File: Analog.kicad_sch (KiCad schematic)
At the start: 32 parts, among them IC1 AMC1350DWVR, IC2 AMC1350DWVR, U3 TLV9001IDBVR, U4 TLV9001IDBVR

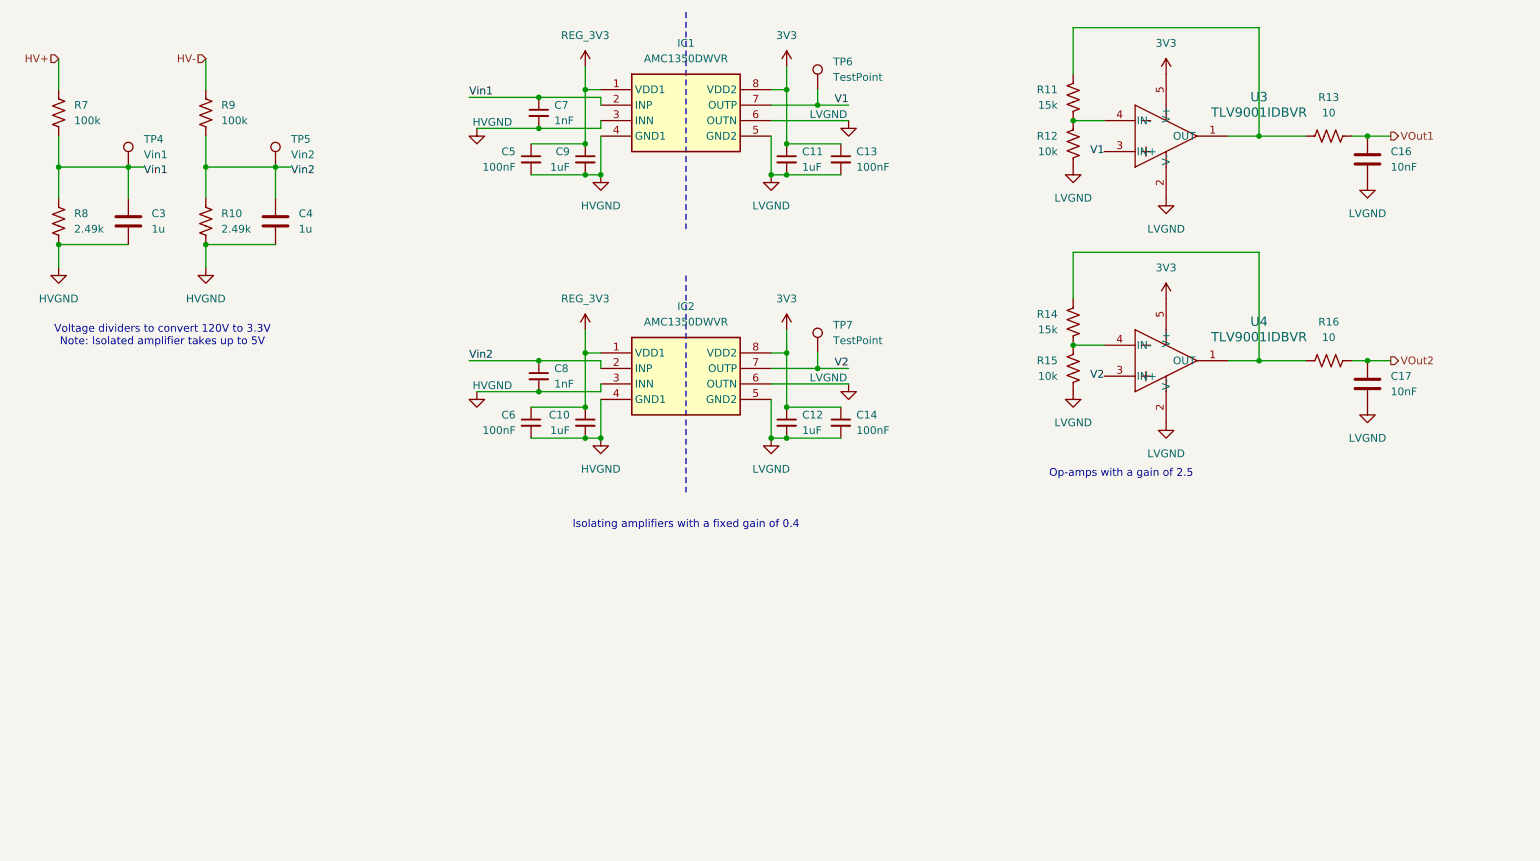
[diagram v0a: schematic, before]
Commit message: With footprints assigned
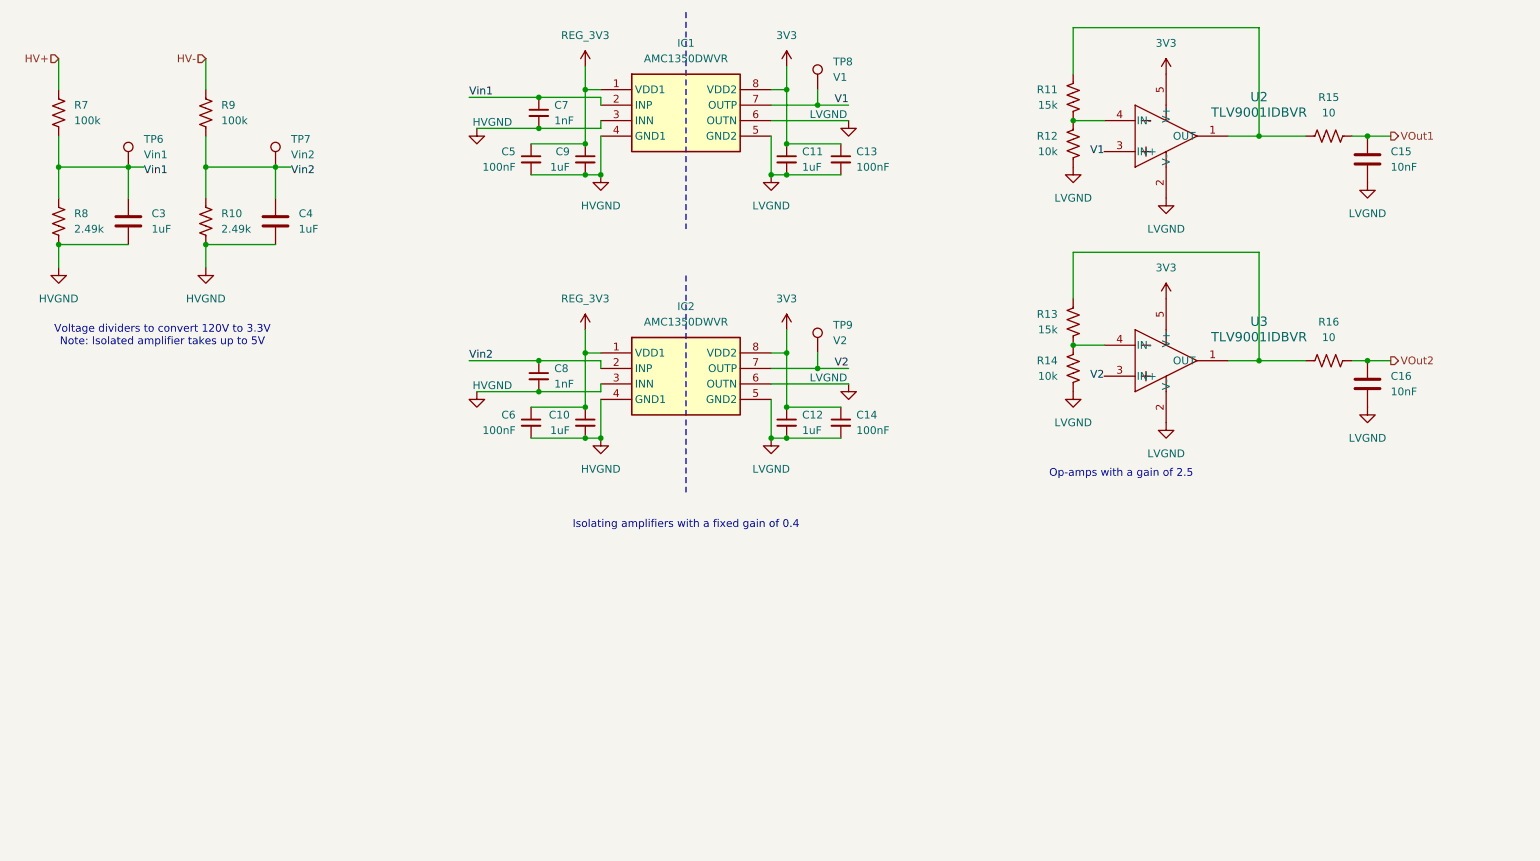
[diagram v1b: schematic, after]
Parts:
- C15: renamed from C16; footprint (none) -> Capacitor_SMD:C_0603_1608Metric_Pad1.08x0.95mm_HandSolder
- C16: renamed from C17; footprint (none) -> Capacitor_SMD:C_0603_1608Metric_Pad1.08x0.95mm_HandSolder
- C3, C4: value 1u -> 1uF; footprint (none) -> Capacitor_SMD:C_0603_1608Metric_Pad1.08x0.95mm_HandSolder
- IC1, IC2: footprint Parts:AMC1350DWVR -> ActivePrecharge-RevB:SOIC127P1150X280-8N
- R10, R11, R12, R7, R8, R9: footprint (none) -> Resistor_SMD:R_0603_1608Metric_Pad0.98x0.95mm_HandSolder
- R13: renamed from R14; footprint (none) -> Resistor_SMD:R_0603_1608Metric_Pad0.98x0.95mm_HandSolder
- R14: renamed from R15; footprint (none) -> Resistor_SMD:R_0603_1608Metric_Pad0.98x0.95mm_HandSolder
- R15: renamed from R13; footprint (none) -> Resistor_SMD:R_0603_1608Metric_Pad0.98x0.95mm_HandSolder; P/N (none) -> CRCW060310R0FKEE
- R16: footprint (none) -> Resistor_SMD:R_0603_1608Metric_Pad0.98x0.95mm_HandSolder; P/N (none) -> CRCW060310R0FKEE
- TP6: renamed from TP4; footprint (none) -> TestPoint:TestPoint_Pad_1.0x1.0mm
- TP7: renamed from TP5; footprint (none) -> TestPoint:TestPoint_Pad_1.0x1.0mm
- TP8: renamed from TP6; value TestPoint -> V1; footprint (none) -> TestPoint:TestPoint_Pad_1.0x1.0mm
- TP9: renamed from TP7; value TestPoint -> V2; footprint (none) -> TestPoint:TestPoint_Pad_1.0x1.0mm
- U2: renamed from U3; footprint DBV0005A_N -> ActivePrecharge-RevB:DBV0005A_N
- U3: renamed from U4; footprint DBV0005A_N -> ActivePrecharge-RevB:DBV0005A_N

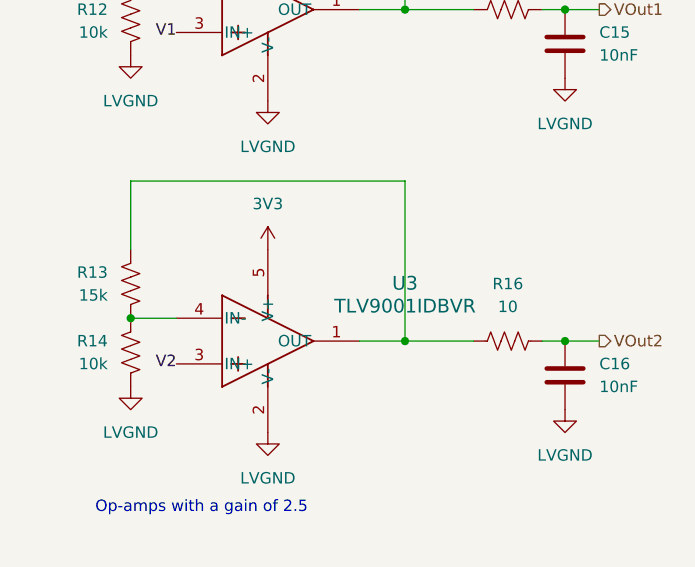
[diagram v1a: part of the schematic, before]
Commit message: Lakshay's comments addressed, still need to move to new branch
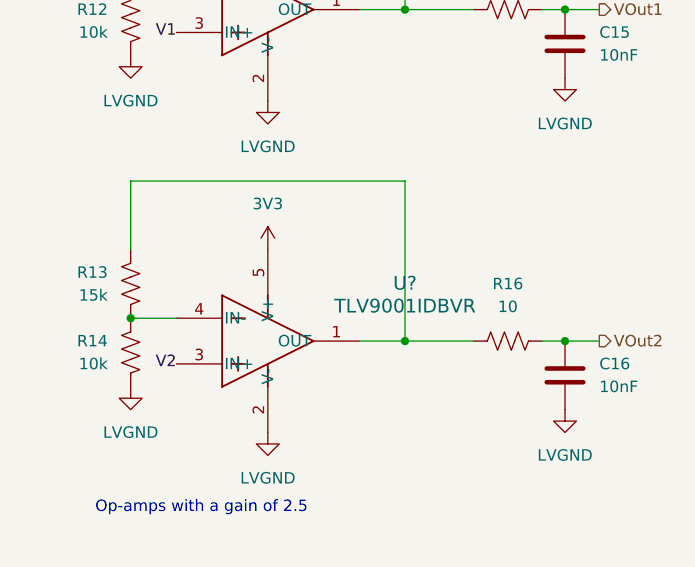
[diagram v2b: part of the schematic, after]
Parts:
- renumbered U3 to U?
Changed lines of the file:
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@@
 		(dnp no)
 		(fields_autoplaced yes)
-		(property "Reference" "U3"
+		(property "Reference" "U?"
 			(at 229.87 76.1298 0)
 			(effects
@@
 		)
 		(instances
-			(project ""
+			(project "ActivePrecharge RevB"
 				(path "/5b79bd62-039b-48b8-a776-6011f31800bf/b87ed4ab-ede8-4401-aaa8-4c2bfd6c5f57"
-					(reference "U3")
+					(reference "U?")
 					(unit 1)
 				)

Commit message: A few minor changes added bc i forgot some stuff
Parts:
- gave numbers to parts that had none: 1
- renumbered C7 to C10, C8 to C11, C9 to C12, C10 to C13, C11 to C14, C12 to C15, C13 to C16, C14 to C17, C15 to C18, C16 to C19, C3 to C6, C4 to C7, C5 to C8, C6 to C9, R9 to R10, R10 to R11, R11 to R12, R12 to R13, R13 to R14, R14 to R15, R15 to R16, R16 to R17, R7 to R8, R8 to R9

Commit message: Last changes addressed with organization changes and the new resolution implementation
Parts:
- removed C18, C19: 10nF, Capacitor_SMD:C_0603_1608Metric_Pad1.08x0.95mm_HandSolder, symbol Device:C
- removed R12, R14: 15k, Resistor_SMD:R_0603_1608Metric_Pad0.98x0.95mm_HandSolder, symbol Device:R_US
- removed R13, R15: 10k, Resistor_SMD:R_0603_1608Metric_Pad0.98x0.95mm_HandSolder, symbol Device:R_US
- removed R16, R17: 10, Resistor_SMD:R_0603_1608Metric_Pad0.98x0.95mm_HandSolder, symbol Device:R_US
- removed U2, U3: TLV9001IDBVR, ActivePrecharge-RevB:DBV0005A_N, symbol 2G5-OPAMP:TLV9001IDBVR
- added C20: 0.1uF, Capacitor_SMD:C_0603_1608Metric_Pad1.08x0.95mm_HandSolder, symbol Device:C_Small
- added C21: 0.47uF, Capacitor_SMD:C_0603_1608Metric_Pad1.08x0.95mm_HandSolder, symbol Device:C_Small
- added C22, C23: 10nF, Capacitor_SMD:C_0603_1608Metric_Pad1.08x0.95mm_HandSolder, symbol Device:C
- added IC3: ZXRE160AET5TA, SOT95P280X100-5N, symbol VREF:ZXRE160AET5TA
- added R18: 1k, Resistor_SMD:R_0603_1608Metric_Pad0.98x0.95mm_HandSolder, symbol Device:R_US
- added R19: 5.1k, Resistor_SMD:R_0603_1608Metric_Pad0.98x0.95mm_HandSolder, symbol Device:R_US
- added R20: 15k, Resistor_SMD:R_0603_1608Metric_Pad0.98x0.95mm_HandSolder, symbol Device:R_US
- added R21, R23, R26, R27: 2.49k, Resistor_SMD:R_0603_1608Metric_Pad0.98x0.95mm_HandSolder, symbol Device:R_US
- added R22, R24, R28, R29: 16k, Resistor_SMD:R_0603_1608Metric_Pad0.98x0.95mm_HandSolder, symbol Device:R_US
- added R25, R30: 10, Resistor_SMD:R_0603_1608Metric_Pad0.98x0.95mm_HandSolder, symbol Device:R_US
- added U4, U5: TLV9001IDBVR, ActivePrecharge-RevB:DBV0005A_N, symbol Simulation_SPICE:OPAMP
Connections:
- net 3V3: now also C20.1, IC3.3 (IN), R18.1, U4.3 (V+), U5.3 (V+)
- net LVGND: now also C20.2, C21.2, C22.2, C23.2, IC3.1 (PGND), IC3.2 (GND), R20.2, R24.2, R28.2, U4.4 (V-), U5.4 (V-)
- net V1: now also R21.1
- net V2: now also R26.1
- net VOut1: now also C22.1, R22.1, R25.1, R25.2, U4.5
- net VOut2: now also C23.1, R29.1, R30.1, R30.2, U5.5
- new net: R23.1, R24.1, U4.2 (-)
- new net: R21.2, R22.2, U4.1 (+)
- new net: R26.2, R29.2, U5.1 (+)
- new net: R27.1, R28.1, U5.2 (-)
- new net REG_0V8: C21.1, IC3.4 (FB), IC3.5 (OUT), R18.2, R19.1, R19.2, R20.1, R23.2, R27.2
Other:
- note added: "Gain And Range Calculations:"
- note added: "Op-amps that subtract an offset of 0.8V and apply a gain of 6.425 to create a 0.34V to 3.36V output range"
- note added: "Output Voltage Range For Dividers:"
- note added: "Voltage dividers to convert 134V to 3.3V Note: Isolated amplifier takes up to 5V"
- note added: "Voltage reference chip that creates a stable 0.8V reference"
- note removed: "Op-amps with a gain of 2.5"
- note removed: "Voltage dividers to convert 120V to 3.3V Note: Isolated amplifier takes up to 5V"
- moved on the sheet: C10, C11, C12, C13, C14, C15, C16, C17, C6, C7, C8, C9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

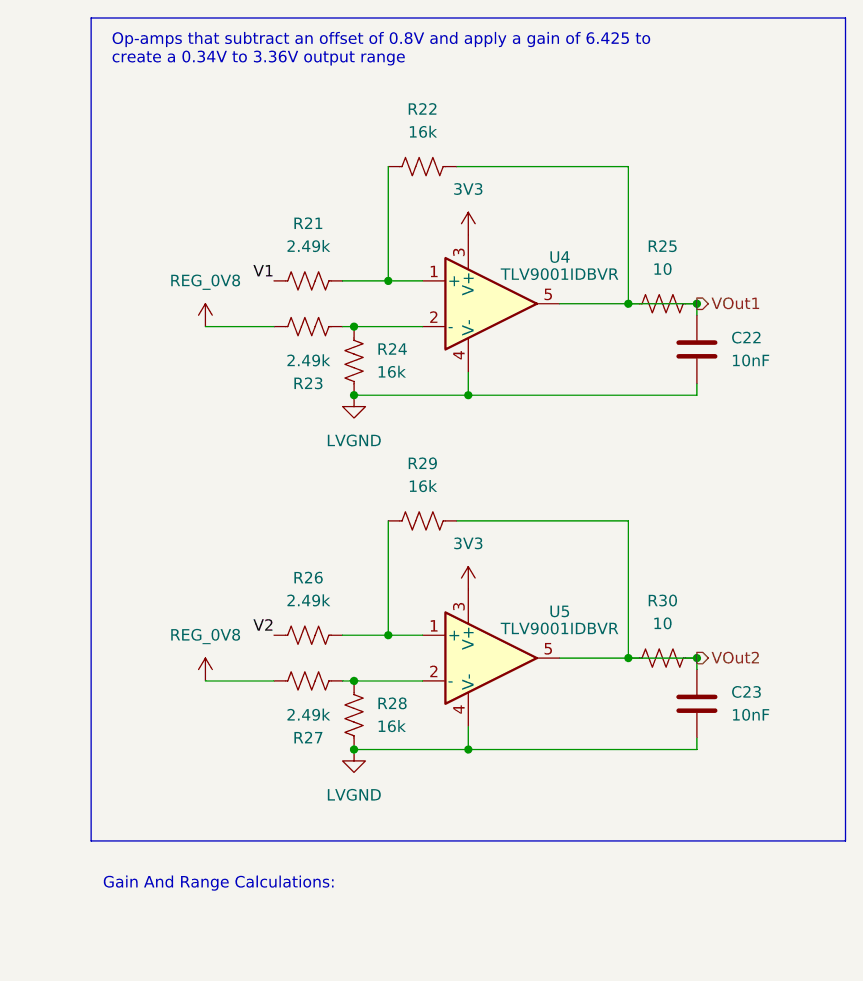
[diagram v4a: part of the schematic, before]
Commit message: Adjustments made after Changxu examined the opamp circuit
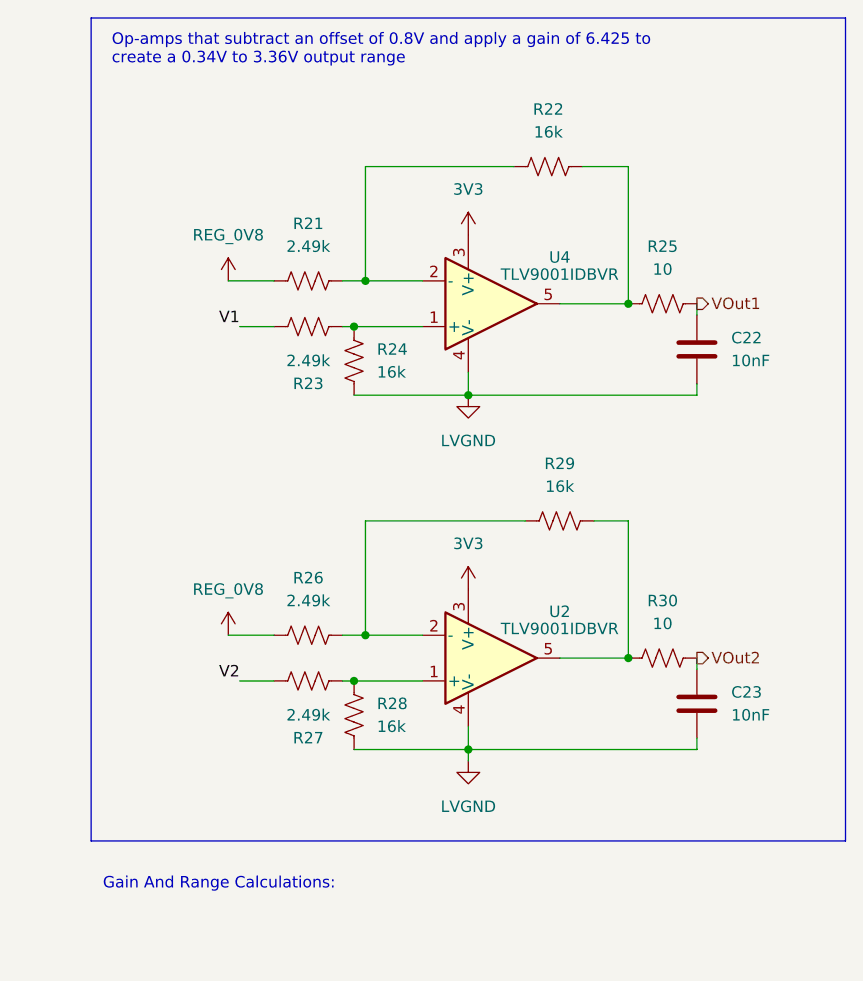
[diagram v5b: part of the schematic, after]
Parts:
- removed U5: TLV9001IDBVR, ActivePrecharge-RevB:DBV0005A_N, symbol Simulation_SPICE:OPAMP
- added U2: TLV9001IDBVR, ActivePrecharge-RevB:DBV0005A_N, symbol Simulation_SPICE:OPAMP
- IC3: footprint SOT95P280X100-5N -> ActivePrecharge-RevB:SOT95P280X100-5N
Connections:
- net 3V3: now also U2.3 (V+)
- net LVGND: now also U2.4 (V-)
- net REG_0V8: now also R21.1, R26.1; no longer R23.2, R27.2
- net V1: now also R23.2; no longer R21.1
- net V2: now also R27.2; no longer R26.1
- net VOut1: no longer R22.1, R25.1, U4.5
- net VOut2: no longer R29.1, R30.1
- net at R23.1, R24.1: now also U4.1 (+); no longer U4.2 (-)
- net at R21.2, R22.2: now also U4.2 (-); no longer U4.1 (+)
- net at R26.2, R29.2: now also U2.2 (-)
- net at R27.1, R28.1: now also U2.1 (+)
- new net: R22.1, R25.1, U4.5
- new net: R29.1, R30.1, U2.5
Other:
- moved on the sheet: R22, R29

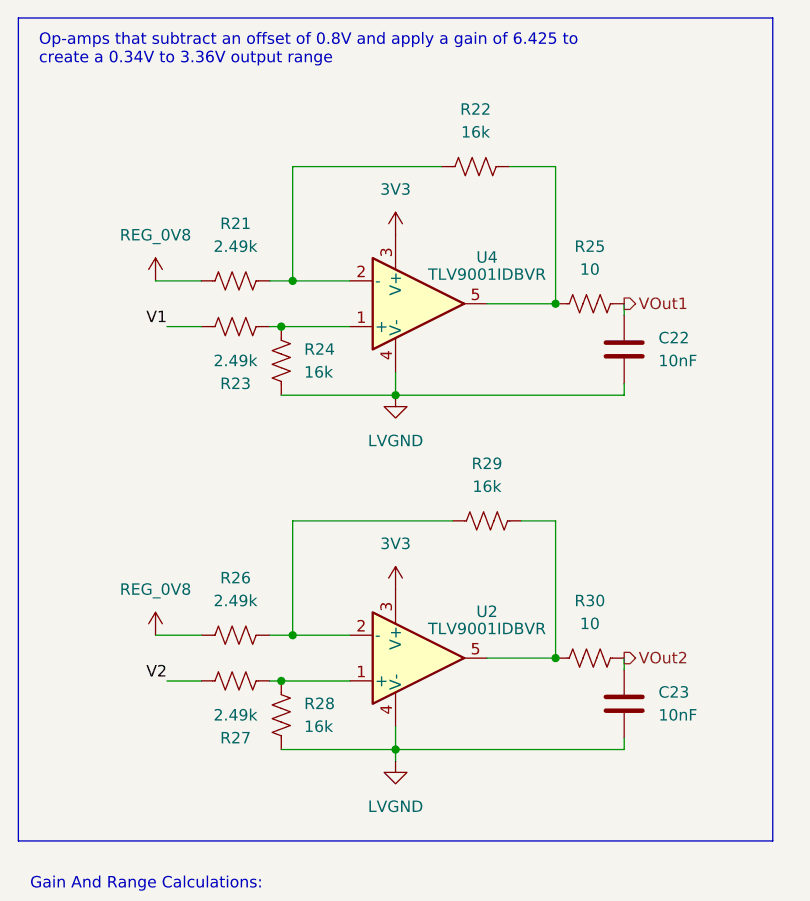
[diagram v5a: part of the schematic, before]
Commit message: Added math for tolerancing on last opamp
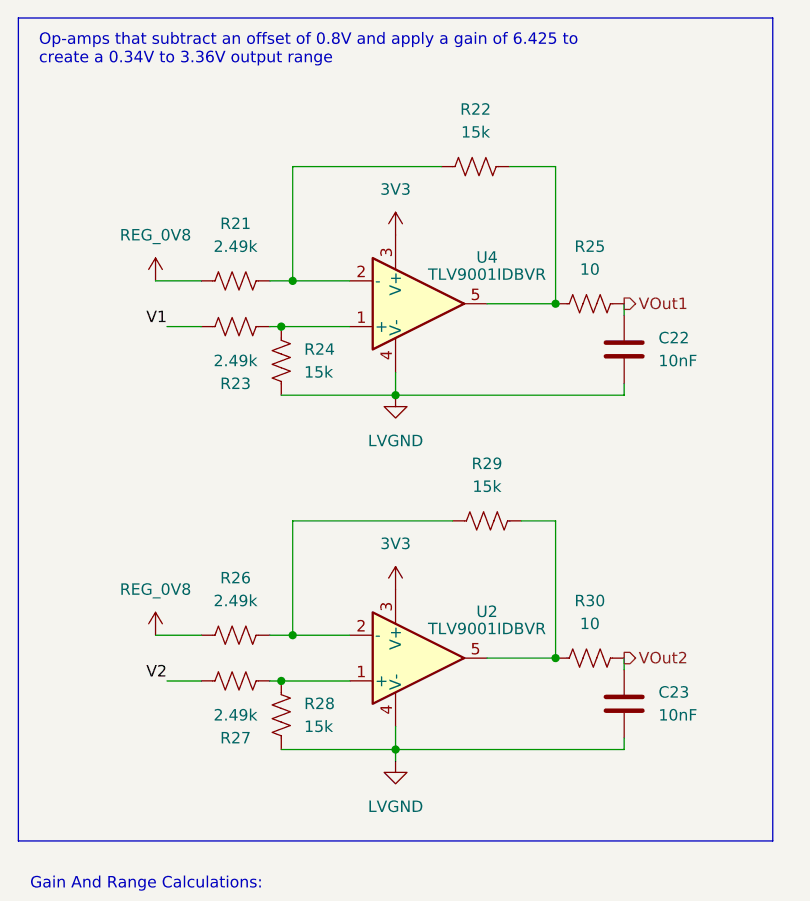
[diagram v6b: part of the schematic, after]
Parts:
- R22, R24, R28, R29: value 16k -> 15k

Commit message: First Initial PCB Layout Finished
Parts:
- renumbered U4 to U2, U2 to U3
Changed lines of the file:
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@@
 		(on_board yes)
 		(dnp no)
-		(property "Reference" "U4"
+		(property "Reference" "U2"
 			(at 240.03 51.9998 0)
 			(do_not_autoplace yes)
@@
 			(project "ActivePrecharge RevB"
 				(path "/5b79bd62-039b-48b8-a776-6011f31800bf/b87ed4ab-ede8-4401-aaa8-4c2bfd6c5f57"
-					(reference "U4")
+					(reference "U2")
 					(unit 1)
 				)
@@
 		(on_board yes)
 		(dnp no)
-		(property "Reference" "U2"
+		(property "Reference" "U3"
 			(at 240.03 91.3698 0)
 			(do_not_autoplace yes)
@@
 			(project "ActivePrecharge RevB"
 				(path "/5b79bd62-039b-48b8-a776-6011f31800bf/b87ed4ab-ede8-4401-aaa8-4c2bfd6c5f57"
-					(reference "U2")
-					(unit 1)
-				)
+					(reference "U3")
+					(unit 1)
+				)
